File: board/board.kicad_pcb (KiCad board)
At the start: 2 copper layers, 91.5 x 68.6 mm, 7 parts, among them J1 Conn_01x25_Socket, J2 Conn_01x01, J2 Conn_01x25_Socket, J3 Conn_01x01, J4 Conn_01x01, J5 Conn_01x01

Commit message: placed components
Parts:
- added J3: ~, TestPoint:TestPoint_Keystone_5019_Minature, F.Cu at (242.4, 97.8)
- added J4: ~, TestPoint:TestPoint_Keystone_5019_Minature, F.Cu at (242.4, 101.7)
- added J5: PJ-320B, project:BOOMELE_PJ-320B, F.Cu at (233.0, 80.8)
- added J6: Screw_Terminal_01x02, 4ms_Connector:Socket_1x02_2.54mm_TH, F.Cu at (249.3, 89.0)
- added J7: Screw_Terminal_01x02, 4ms_Connector:Socket_1x02_2.54mm_TH, F.Cu at (253.9, 89.0)
- added J8: Screw_Terminal_01x02, 4ms_Connector:Socket_1x02_2.54mm_TH, F.Cu at (258.5, 89.0)
- added R1: 3.0k_0603_0.1%, 4ms_Resistor:R_0603, F.Cu at (226.6, 89.3)
- added R10: 1k_0603_0.1%, 4ms_Resistor:R_0603, F.Cu at (230.8, 99.5)
- added R11: 100k_0603, 4ms_Resistor:R_0603, F.Cu at (235.1, 89.3)
- added R12: 100k_0603, 4ms_Resistor:R_0603, F.Cu at (235.1, 91.8)
- added R13: 1k_0603_0.1%, 4ms_Resistor:R_0603, F.Cu at (235.1, 94.4)
- added R14: 100k_0603, 4ms_Resistor:R_0603, F.Cu at (235.1, 96.9)
- added R15: 1k_0603_0.1%, 4ms_Resistor:R_0603, F.Cu at (235.1, 99.5)
- added R2: 3.0k_0603_0.1%, 4ms_Resistor:R_0603, F.Cu at (226.6, 91.8)
- added R3: 3.0k_0603_0.1%, 4ms_Resistor:R_0603, F.Cu at (226.6, 94.4)
- added R4: 3.0k_0603_0.1%, 4ms_Resistor:R_0603, F.Cu at (226.6, 96.9)
- added R5: 3.0k_0603_0.1%, 4ms_Resistor:R_0603, F.Cu at (226.6, 99.5)
- added R6: 3.0k_0603_0.1%, 4ms_Resistor:R_0603, F.Cu at (230.8, 89.3)
- added R7: 3.0k_0603_0.1%, 4ms_Resistor:R_0603, F.Cu at (230.8, 91.8)
- added R8: 1k_0603_0.1%, 4ms_Resistor:R_0603, F.Cu at (230.8, 94.4)
- added R9: 2.2k_0603, 4ms_Resistor:R_0603, F.Cu at (230.8, 96.9)
- added U1: ~, Package_SO:SOIC-8_3.9x4.9mm_P1.27mm, F.Cu at (251.2, 97.1)
- added U10: ~, Package_SO:SOIC-16W_7.5x10.3mm_P1.27mm, F.Cu at (201.9, 85.9)
- added U11: ~, 4ms_Package_DIP:DIP-8pin_TH, F.Cu at (241.3, 76.9)
- added U12: ~, project:W25Q128_board, F.Cu at (210.4, 83.0)
- added U13: ~, 4ms_Package_DIP:DIP-8pin_TH, F.Cu at (252.5, 76.9)
- added U14: ~, Package_SO:SOIC-16W_7.5x10.3mm_P1.27mm, F.Cu at (201.9, 97.8)
- added U2: ~, project:AD9833, F.Cu at (210.4, 65.3)
- added U3: ~, project:AD9833, F.Cu at (224.7, 65.3)
- added U4: ~, project:AD9833, F.Cu at (239.1, 65.3)
- added U5: ~, project:AD9833, F.Cu at (253.4, 65.3)
- added U6: ~, Package_SO:VSSOP-10_3x3mm_P0.5mm, F.Cu at (243.3, 88.9)
- added U7: ~, Package_SO:VSSOP-10_3x3mm_P0.5mm, F.Cu at (243.3, 93.5)
- added U8: ~, Package_SO:SOIC-16W_7.5x10.3mm_P1.27mm, F.Cu at (201.9, 61.9)
- added U9: ~, Package_SO:SOIC-16W_7.5x10.3mm_P1.27mm, F.Cu at (201.9, 73.9)
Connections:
- J1 pad 10: /PC8 -> ZCEN_3
- J1 pad 11: /PC7 -> ZCEN_2
- J1 pad 12: /PC6 -> ZCEN_1
- J1 pad 13: /PB15/adc4_in5 -> Analog_data
- J1 pad 14: /PB14/adc4_in4 -> FLASH_CS
- J1 pad 15: /PB13/adc3_in5 -> Analog_CLK
- J1 pad 16: /PB12/adc4_in3 -> MUX_SEL_4
- J1 pad 17: /PB11 -> MUX_SEL_2
- J1 pad 18: /PB10 -> MUX_SEL_3
- J1 pad 19: /PB2 -> NOISE_CLK_SEL
- J1 pad 20: /PB1/adc3_in1 -> PWM3
- J1 pad 21: /PB0/adc3_in12 -> PWM1
- J1 pad 6: /PA10 -> CS_AD9833_3
- J1 pad 7: /PA9 -> CS_AD9833_2
- J1 pad 9: /PC9 -> ZCEN_DAC
- J2 pad 10: /PB6 -> PWM2
- J2 pad 11: /PB7 -> NOISE_CLK
- J2 pad 12: /PB8 -> FILT_CLK
- J2 pad 13: /PB9 -> NOISE_DI
- J2 pad 14: /PC13 -> MUX_SEL_1
- J2 pad 20: /PA1 -> PWM4
- J2 pad 21: /PA2 -> ATTEN_CS
- J2 pad 22: /PA3 -> CS_AD9833_1
- J2 pad 4: /PA15 -> NOISE_CS
- J2 pad 5: /PC12 -> CS_AD9833_4
- J2 pad 7: /PB3 -> FLASH_CLK
- J2 pad 8: /PB4 -> FLASH_MISO
- J2 pad 9: /PB5 -> FLASH_MOSI

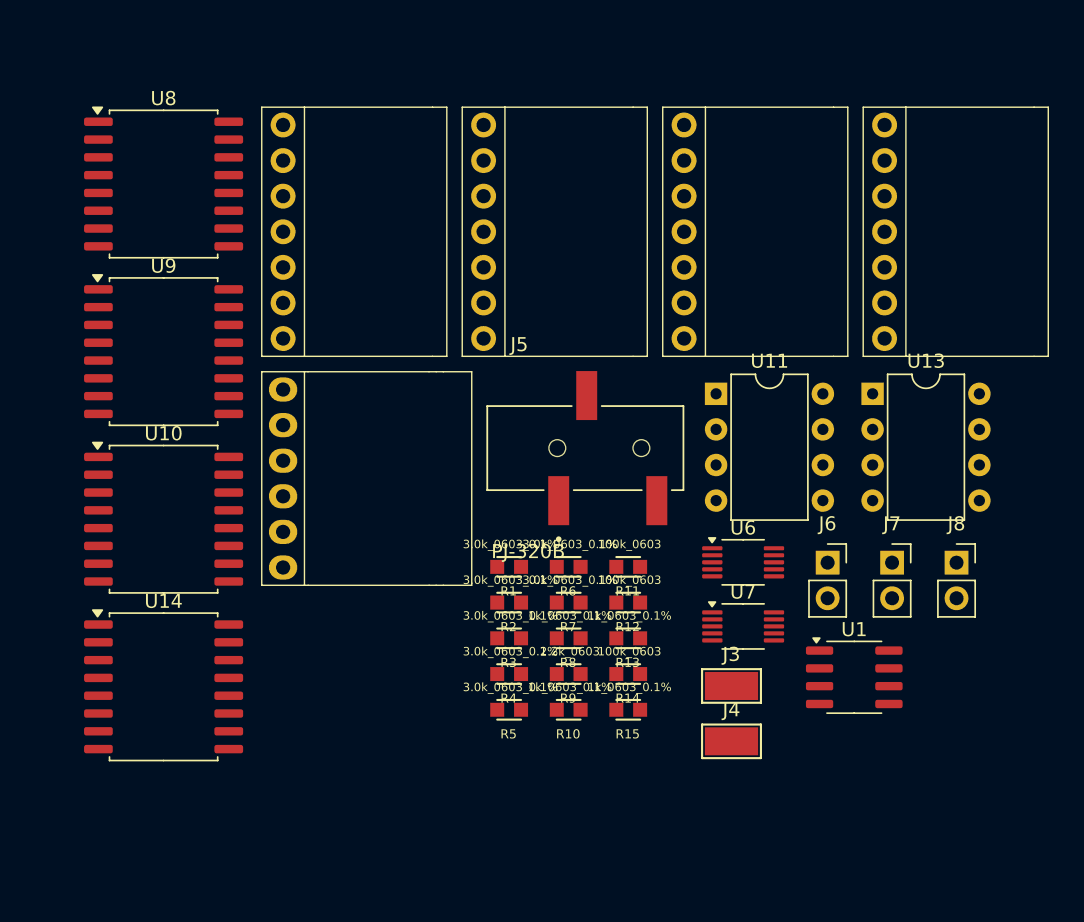
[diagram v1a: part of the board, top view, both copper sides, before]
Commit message: add Ux reference to boards and place components again...
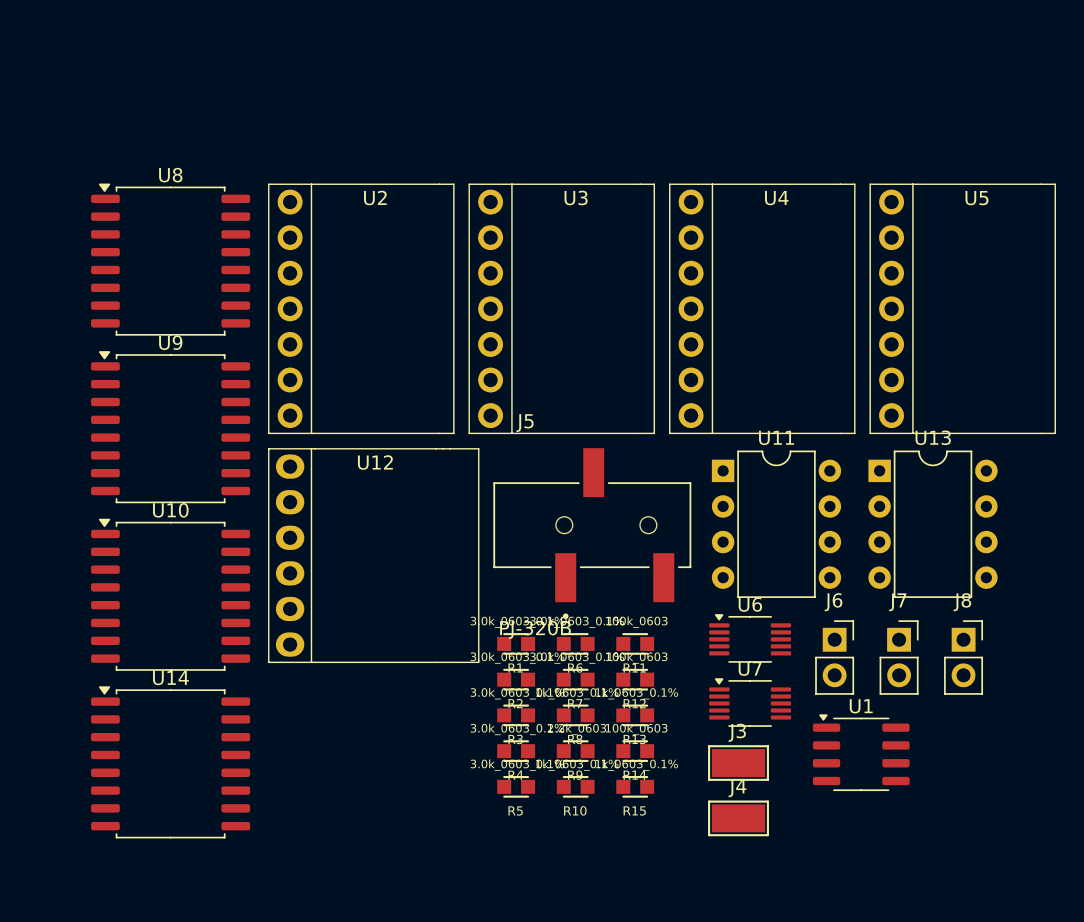
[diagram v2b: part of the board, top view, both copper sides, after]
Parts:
- moved J3 5.52 mm to (242.9, 103.3)
- moved J4 5.52 mm to (242.9, 107.2)
- moved J5 5.52 mm to (233.5, 86.3)
- moved J6 5.52 mm to (249.8, 94.5)
- moved J7 5.52 mm to (254.4, 94.5)
- moved J8 5.52 mm to (259.0, 94.5)
- moved R1 5.52 mm to (227.1, 94.8)
- moved R10 5.52 mm to (231.3, 105.0)
- moved R11 5.52 mm to (235.6, 94.8)
- moved R12 5.52 mm to (235.6, 97.3)
- moved R13 5.52 mm to (235.6, 99.9)
- moved R14 5.52 mm to (235.6, 102.4)
- moved R15 5.52 mm to (235.6, 105.0)
- moved R2 5.52 mm to (227.1, 97.3)
- moved R3 5.52 mm to (227.1, 99.9)
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
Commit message: horrible attempt at placing components
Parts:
- R13, R15, U4, U5: moved to B.Cu
- moved J4 143.0 mm to (111.0, 52.0)
- moved J3 139.8 mm to (111.0, 57.0)
- moved U11 130.1 mm to (113.2, 101.8), turned to 90 degrees
- moved U6 123.1 mm to (125.0, 62.0), turned to 180 degrees
- moved U4 115.5 mm to (124.0, 70.5), turned to -90 degrees
- moved U5 109.7 mm to (144.5, 78.9), turned to -90 degrees
- moved U13 103.0 mm to (150.4, 91.6), turned to 90 degrees
- moved R11 101.9 mm to (133.8, 99.8)
- moved U7 96.9 mm to (152.0, 68.0), turned to 90 degrees
- moved R15 94.1 mm to (143.2, 87.0), turned to 180 degrees
- moved R12 92.8 mm to (142.8, 99.8)
- moved U1 89.7 mm to (169.0, 68.0), turned to 90 degrees
- moved R13 88.6 mm to (147.0, 97.0), turned to 90 degrees
- moved U2 87.0 mm to (124.0, 67.1), turned to 90 degrees
- moved U3 80.9 mm to (144.5, 75.0), turned to 90 degrees
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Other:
- board text added: "DAC out"

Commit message: add caps on power lines, start tracing
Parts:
- added C1: 0.22uF_0603_25V, 4ms_Capacitor:C_0603, B.Cu at (167.0, 68.0)
- added C10: 0.22uF_0603_25V, 4ms_Capacitor:C_0603, B.Cu at (151.0, 101.0)
- added C11: 0.22uF_0603_25V, 4ms_Capacitor:C_0603, B.Cu at (157.0, 101.0)
- added C12: 0.22uF_0603_25V, 4ms_Capacitor:C_0603, B.Cu at (169.0, 87.0)
- added C13: 0.22uF_0603_25V, 4ms_Capacitor:C_0603, F.Cu at (172.0, 61.0)
- added C14: 0.22uF_0603_25V, 4ms_Capacitor:C_0603, B.Cu at (152.0, 62.0)
- added C15: 0.22uF_0603_25V, 4ms_Capacitor:C_0603, F.Cu at (118.0, 105.0)
- added C16: 0.22uF_0603_25V, 4ms_Capacitor:C_0603, B.Cu at (173.0, 87.0)
- added C17: 0.22uF_0603_25V, 4ms_Capacitor:C_0603, B.Cu at (138.0, 82.0)
- added C18: 0.22uF_0603_25V, 4ms_Capacitor:C_0603, B.Cu at (154.0, 101.0)
- added C19: 0.22uF_0603_25V, 4ms_Capacitor:C_0603, B.Cu at (143.0, 86.0)
- added C2: 0.22uF_0603_25V, 4ms_Capacitor:C_0603, F.Cu at (133.0, 79.0)
- added C20: 0.22uF_0603_25V, 4ms_Capacitor:C_0603, B.Cu at (140.0, 64.0)
- added C21: 0.22uF_0603_25V, 4ms_Capacitor:C_0603, B.Cu at (155.0, 89.0)
- added C22: 0.22uF_0603_25V, 4ms_Capacitor:C_0603, F.Cu at (113.0, 67.0)
- added C23: 0.22uF_0603_25V, 4ms_Capacitor:C_0603, B.Cu at (142.0, 67.0)
- added C3: 0.22uF_0603_25V, 4ms_Capacitor:C_0603, F.Cu at (116.0, 75.0)
- added C4: 0.22uF_0603_25V, 4ms_Capacitor:C_0603, F.Cu at (119.0, 62.0)
- added C5: 0.22uF_0603_25V, 4ms_Capacitor:C_0603, F.Cu at (133.0, 75.0)
- added C6: 0.22uF_0603_25V, 4ms_Capacitor:C_0603, F.Cu at (141.0, 96.0)
- added C7: 0.22uF_0603_25V, 4ms_Capacitor:C_0603, B.Cu at (156.0, 80.0)
- added C8: 0.22uF_0603_25V, 4ms_Capacitor:C_0603, F.Cu at (171.0, 97.0)
- added C9: 0.22uF_0603_25V, 4ms_Capacitor:C_0603, B.Cu at (144.0, 64.0)
- R11: moved to B.Cu
- moved R11 13.8 mm to (139.0, 87.0), turned to 180 degrees
- moved R15 3.80 mm to (146.8, 88.0)
- moved R1 2.00 mm to (157.0, 65.0)
- moved R10 2.00 mm to (170.1, 75.0)
- moved R2 2.00 mm to (157.0, 68.0)
- moved R3 2.00 mm to (157.0, 71.0)
- moved R4 2.00 mm to (157.0, 74.0)
- moved R5 2.00 mm to (161.2, 65.0)
- moved R6 2.00 mm to (161.2, 68.0)
- moved R7 2.00 mm to (161.2, 71.0)
- moved R8 2.00 mm to (164.0, 75.0)
- moved R9 2.00 mm to (167.1, 75.0)
- moved U1 2.00 mm to (167.0, 68.0)
- moved U12 2.00 mm to (163.0, 62.0)
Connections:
- J1 pad 14: FLASH_CS -> /PB14/adc4_in4
- J2 pad 6: /PD2 -> FLASH_CS
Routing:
- net Analog_CLK: track 0.00 -> 112.4 mm, vias 0 -> 6
- net CS_AD9833_2: track 0.00 -> 78.6 mm
- net Analog_data: track 0.00 -> 65.9 mm, vias 0 -> 4
- net CS_AD9833_3: track 0.00 -> 46.1 mm
- net CS_AD9833_4: track 0.00 -> 40.8 mm
- net Analog_data_out1: track 0.00 -> 29.0 mm, vias 0 -> 2
- net Analog_data_out2: track 0.00 -> 19.7 mm, vias 0 -> 2
- net Analog_data_out3: track 0.00 -> 18.6 mm, vias 0 -> 3
- net CS_AD9833_1: track 0.00 -> 18.2 mm
- net FLASH_MISO: track 0.00 -> 13.5 mm
- net FLASH_CLK: track 0.00 -> 10.3 mm
- net FLASH_MOSI: track 0.00 -> 9.28 mm
- net FLASH_CS: track 0.00 -> 8.67 mm

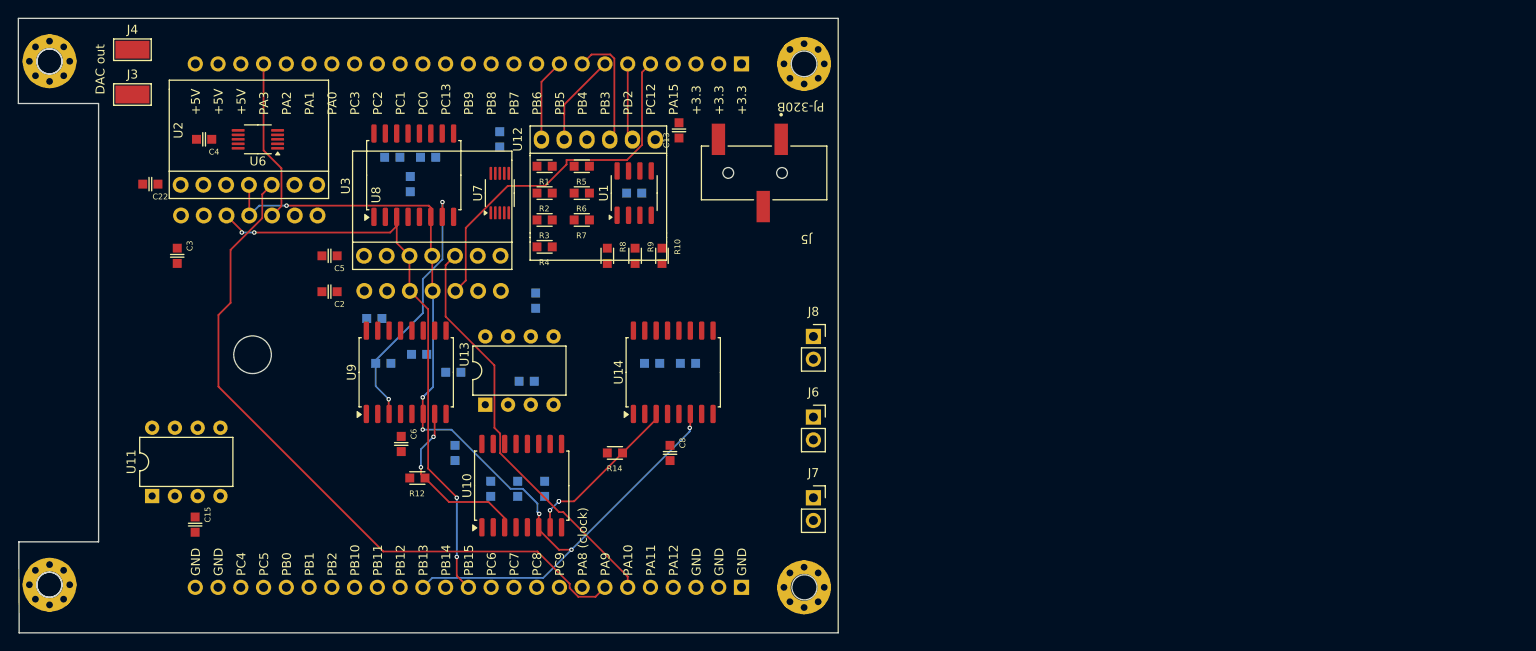
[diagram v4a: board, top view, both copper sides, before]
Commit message: traced (changed some CS and mux select pins to make tracing easier)
Dude that's horrible PCB...
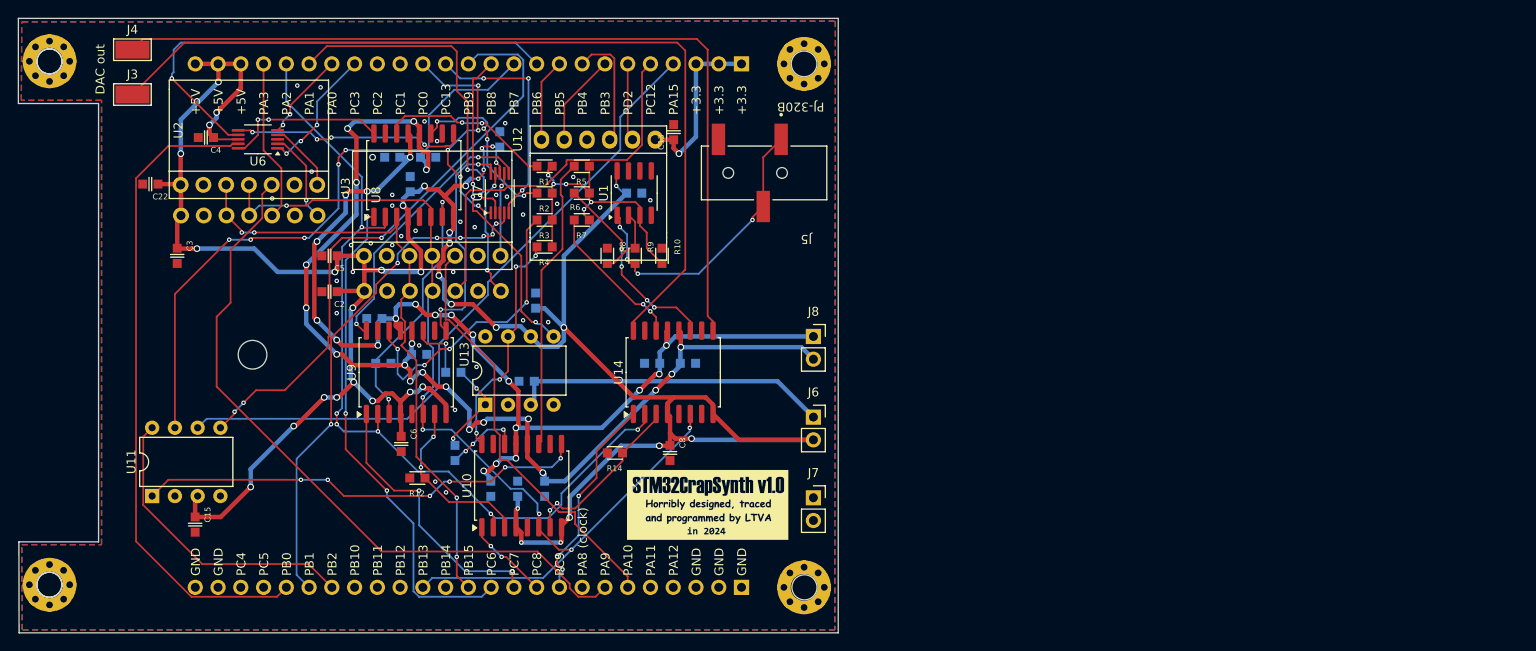
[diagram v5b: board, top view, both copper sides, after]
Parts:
- added G***: LOGO, project:logo_negative, F.Cu at (175.2, 102.8)
- moved C13 0.63 mm to (171.4, 61.2)
- moved C4 0.28 mm to (119.2, 61.8)
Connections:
- J1 pad 16: MUX_SEL_4 -> /PB12/adc4_in3
- J1 pad 17: MUX_SEL_2 -> /PB11
- J1 pad 18: MUX_SEL_3 -> /PB10
- J2 pad 14: MUX_SEL_1 -> MUX_SEL_3
- J2 pad 15: /PC0 -> MUX_SEL_4
- J2 pad 18: /PC3 -> MUX_SEL_1
- J2 pad 19: /PA0 -> MUX_SEL_2
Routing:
- net +5V: track 0.00 -> 305.3 mm, vias 0 -> 38
- net P,+15: track 0.00 -> 125.3 mm, vias 0 -> 19
- net P,-15: track 0.00 -> 116.3 mm, vias 0 -> 20
- net DAC_tovol2: track 0.00 -> 98.1 mm
- net ATTEN_CS: track 0.00 -> 97.1 mm, vias 0 -> 6
- net DAC_tovol1: track 0.00 -> 96.8 mm
- net NOISE_CS: track 0.00 -> 75.7 mm
- net PWM1: track 0.00 -> 73.3 mm
- net NOISE_CLK: track 0.00 -> 68.8 mm, vias 0 -> 5
- net NOISE_DI: track 0.00 -> 66.3 mm, vias 0 -> 3
- net PWM3: track 0.00 -> 57.3 mm, vias 0 -> 7
- net ZCEN_1: track 0.00 -> 56.1 mm, vias 0 -> 3
- net PWM2: track 0.00 -> 55.1 mm, vias 0 -> 1
- net NOISE_TOVOL: track 0.00 -> 50.5 mm, vias 0 -> 6
- net PWM4: track 0.00 -> 38.8 mm, vias 0 -> 2
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- added copper zone on B.Cu, net GND
- added copper zone on F.Cu, net GND
